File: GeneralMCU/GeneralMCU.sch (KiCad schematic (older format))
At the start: 75 parts, among them J1 ARM_JTAG_SWD, J2 Conn_01x03, J3 USB_B_Micro, J4 Conn_01x04, J5 PWR, J6 OLED, SW1 USER, SW2 RESET, U1 STM32F303R6Tx, U2 SN65HVD230, U3 AZ1117-3.3, Y1 32.768kHz, Y2 8MHz

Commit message: Schematic getting toasty.
99% Percent of symbols added with 90% of footprints filled in, 30% of parts spec'd.

Layout organized by functional group
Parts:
- removed J2: Conn_01x03, symbol Connector_Generic:Conn_01x03
- removed SW1: USER, symbol Switch:SW_Push_Dual
- added C33: 10u, µ104KiCAD_RLC:SMD_pkg_1206, symbol Device:C_Small
- added C34, C35: 1u, µ104KiCAD_RLC:SMD_pkg_0603, symbol Device:C_Small
- added C36: 0.1u, µ104KiCAD_RLC:SMD_pkg_0603, symbol Device:C_Small
- added D6: 5V, LEDs:LED_0603, symbol Device:LED
- added D7: +V, LEDs:LED_0603, symbol Device:LED
- added D8: USB, LEDs:LED_0603, symbol Device:LED
- added D9: ISO5, LEDs:LED_0603, symbol Device:LED
- added F2: 500mA PTC, Diodes_SMD:D_1206, symbol Device:Fuse_Small
- added FB2: FB, µ104KiCAD_RLC:SMD_pkg_0805, symbol Device:Ferrite_Bead_Small
- added JP3: Jumper_NC_Small, Pin_Headers:Pin_Header_Straight_1x02_Pitch2.54mm_SMD_Pin1Left, symbol Device:Jumper_NC_Small
- added Q1: Q_NMOS_DGS, TO_SOT_Packages_SMD:SOT-23, symbol Device:Q_NMOS_GSD
- added R10, R9: 1k, µ104KiCAD_RLC:SMD_pkg_0603, symbol Device:R_Small_US
- added R11, R18, R19, R20, R21: 0, µ104KiCAD_RLC:SMD_pkg_0603, symbol Device:R_Small_US
- added R12, R13, R14, R15, R16, R17: 10k, µ104KiCAD_RLC:SMD_pkg_0603, symbol Device:R_Small_US
- added R22, R23: 4.7k, µ104KiCAD_RLC:SMD_pkg_0603, symbol Device:R_Small_US
- added SW1: USER, Buttons_Switches_SMD:SW_SPST_B3U-1000P, symbol Switch:SW_Push
- added TP2: GND, Measurement_Points:Measurement_Point_Round-SMD-Pad_Small, symbol Connector:TestPoint
- added TP3: 5V, Measurement_Points:Measurement_Point_Round-SMD-Pad_Small, symbol Connector:TestPoint
- added TP4: ISOGND, Measurement_Points:Measurement_Point_Round-SMD-Pad_Small, symbol Connector:TestPoint
- added TP5: +V, Measurement_Points:Measurement_Point_Round-SMD-Pad_Small, symbol Connector:TestPoint
- added TP6: USB, Measurement_Points:Measurement_Point_Round-SMD-Pad_Small, symbol Connector:TestPoint
- added TP7: 5V ISO, Measurement_Points:Measurement_Point_Round-SMD-Pad_Small, symbol Connector:TestPoint
- added U4: P78E05-1000, symbol u104_KICAD_dcdc:V_REG
- added U5: BME280, µ104KiCAD_IC:SOT-363-6, symbol u104_KICAD_sensor:BME280
- added U6: R2S-IIOO-R, symbol u104_KICAD_dcdc:R2S-IIOO-R
- BZ1: footprint (none) -> Buzzer_Beeper:Buzzer_Murata_PKMCS0909E4000-R1
- C1, C10, C11, C12, C13, C14, C15, C16, C17, C18, C19, C2, C20, C21, C3, C30, C31, C4, C5, C6, C7, C8, C9: footprint Capacitors_SMD:C_0603 -> µ104KiCAD_RLC:SMD_pkg_0603
- C22, C23: footprint Capacitors_SMD:C_0603 -> (none)
- C24, C25, C26, C27, C29, C32: footprint Capacitors_SMD:C_1206 -> µ104KiCAD_RLC:SMD_pkg_1206
- C28: value 10u -> 22u; footprint Capacitors_SMD:C_1206 -> µ104KiCAD_RLC:SMD_pkg_1206
- D1: value LED -> 3V3
- D2: footprint LED_SMD:LED_WS2812B_PLCC4_5.0x5.0mm_P3.2mm -> LEDs:LED_WS2812-PLCC6; symbol LED:WS2812B -> LED:WS2812
- FB1: footprint (none) -> µ104KiCAD_RLC:SMD_pkg_0805
- H1, H2, H3, H4: footprint MountingHole:MountingHole_3.2mm_M3_Pad -> (none)
- J3: footprint (none) -> Connectors_USB:USB_Micro-B_Wuerth-629105150521_CircularHoles
- J5: footprint (none) -> Pin_Headers:Pin_Header_Straight_1x02_Pitch2.54mm_SMD_Pin1Left
- J6: footprint (none) -> Pin_Headers:Pin_Header_Straight_1x04_Pitch2.54mm_SMD_Pin1Left
- JP1, JP2: footprint Pin_Headers:Pin_Header_Straight_1x02_Pitch2.54mm -> µ104KiCAD:JUMPER_EGG
- L1: footprint (none) -> µ104KiCAD_RLC:SMD_pkg_1210
- R1, R2, R3, R4, R5, R6: footprint Resistors_SMD:R_0603 -> µ104KiCAD_RLC:SMD_pkg_0603
- R7, R8: footprint Resistors_SMD:R_0603 -> µ104KiCAD_RLC:SMD_pkg_1210
- SB1, SB2, SB3, SB4: footprint µ104KiCAD:JUMPER_EGG -> (none)
- SB5: footprint (none) -> µ104KiCAD:JUMPER_EGG
- SW2: footprint (none) -> Buttons_Switches_SMD:SW_SPST_B3U-1000P; symbol Switch:SW_Push_Dual -> Switch:SW_Push
- TP1: value TestPoint -> 3V3; footprint (none) -> Measurement_Points:Measurement_Point_Round-SMD-Pad_Small
- U3: footprint (none) -> TO_SOT_Packages_SMD:SOT-223-3_TabPin2
- Y1: footprint (none) -> µ104KiCAD_IC:Crystal_NDK_NX3215SA
- Y2: footprint (none) -> µ104KiCAD_IC:Crystal_L5_W3.2
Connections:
- net labels added: VBUS
- wire segments 254 -> 311
- no-connect marks 0 -> 5
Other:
- note added: "- screen and bme280.\n- check nucleo and ref designs\n- make layout like esp or rfm69 modules with solderable pads\n"
- note added: "Drop In PCB Spec:\n1) CAN - Place TVS diode and bus filter caps close to CAN connector\n\n"
- note added: "PARADUINO"
- note added: "PKG\n\n"
- note removed: "- update u104 footprints to new lib\n- check nucleo and ref designs\n- make layout like esp or rfm69 modules with solderable pads\n"
- note removed: "Module\n\n\n"
- note removed: "Node Shield Outline\nOne Node template of a stm32 nucleo shield with all this stuff already on it that we can use for all our designs.\n\n24V Input, all protections\nPower LEDs, RGB User LED\nReset Button, User Button\nSWD Programming Header, Can Term, USB Power Jumpers\nWatchdog, CAN, Piezo, whatever SW wants.\n*Lantronix Eth\n*RS232\n*MicroSD\n*2 Mb EEPROM\n*Loadswitch\n*Possible local Screen.\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"
- note removed: "Receving PCB Spec:\n1) Place TVS diode and bus filter caps close to CAN connector\n\n"
- note removed: "Test Points and LEDs"
- moved on the sheet: BZ1, C24, C26, C28, C29, C30, C31, C32, J1, J3, J6, L1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

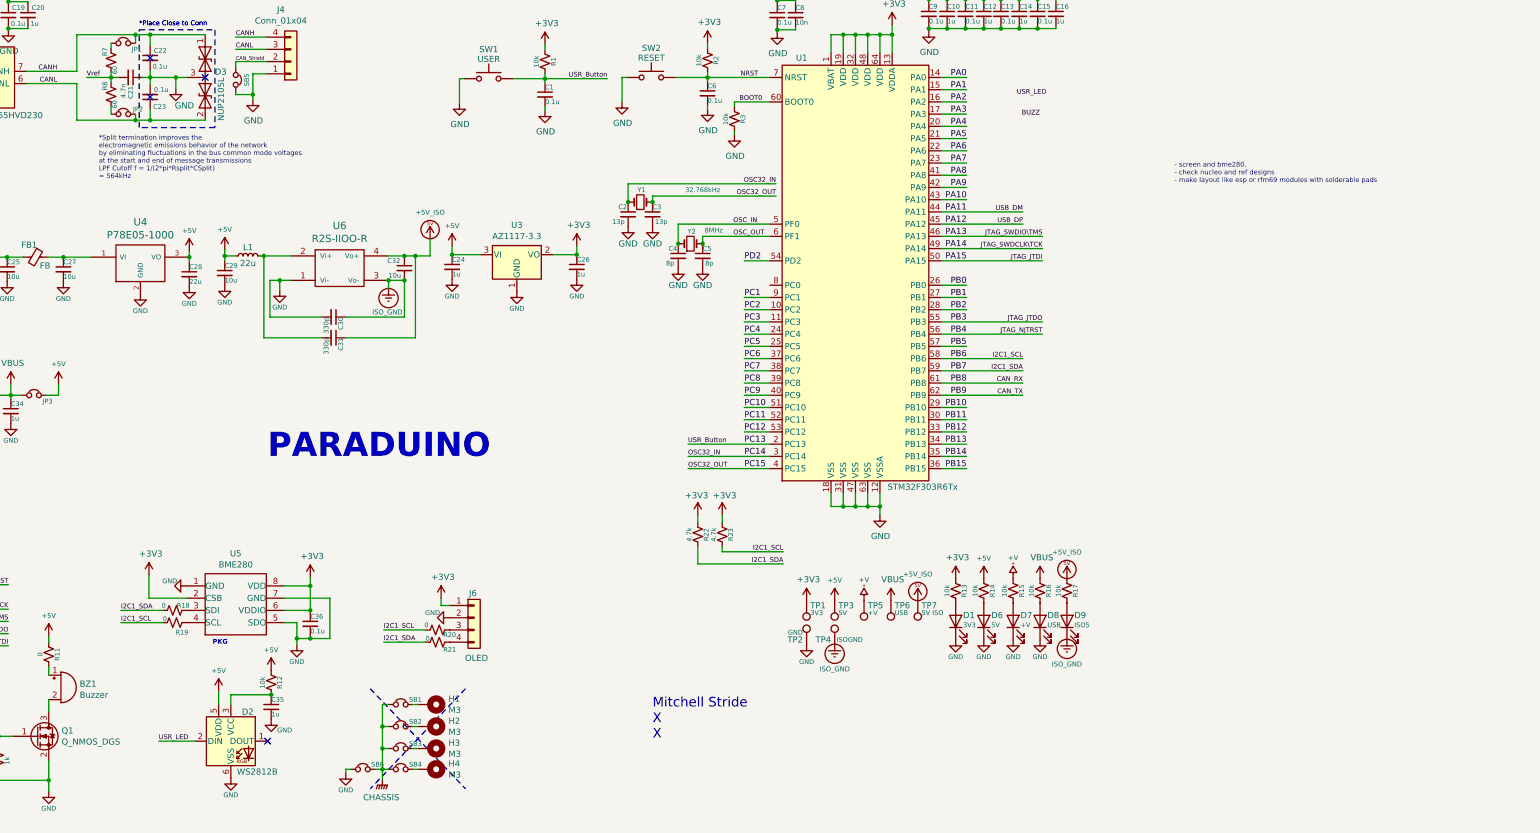
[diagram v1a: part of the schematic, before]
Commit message: Needs castellated pads and sch review
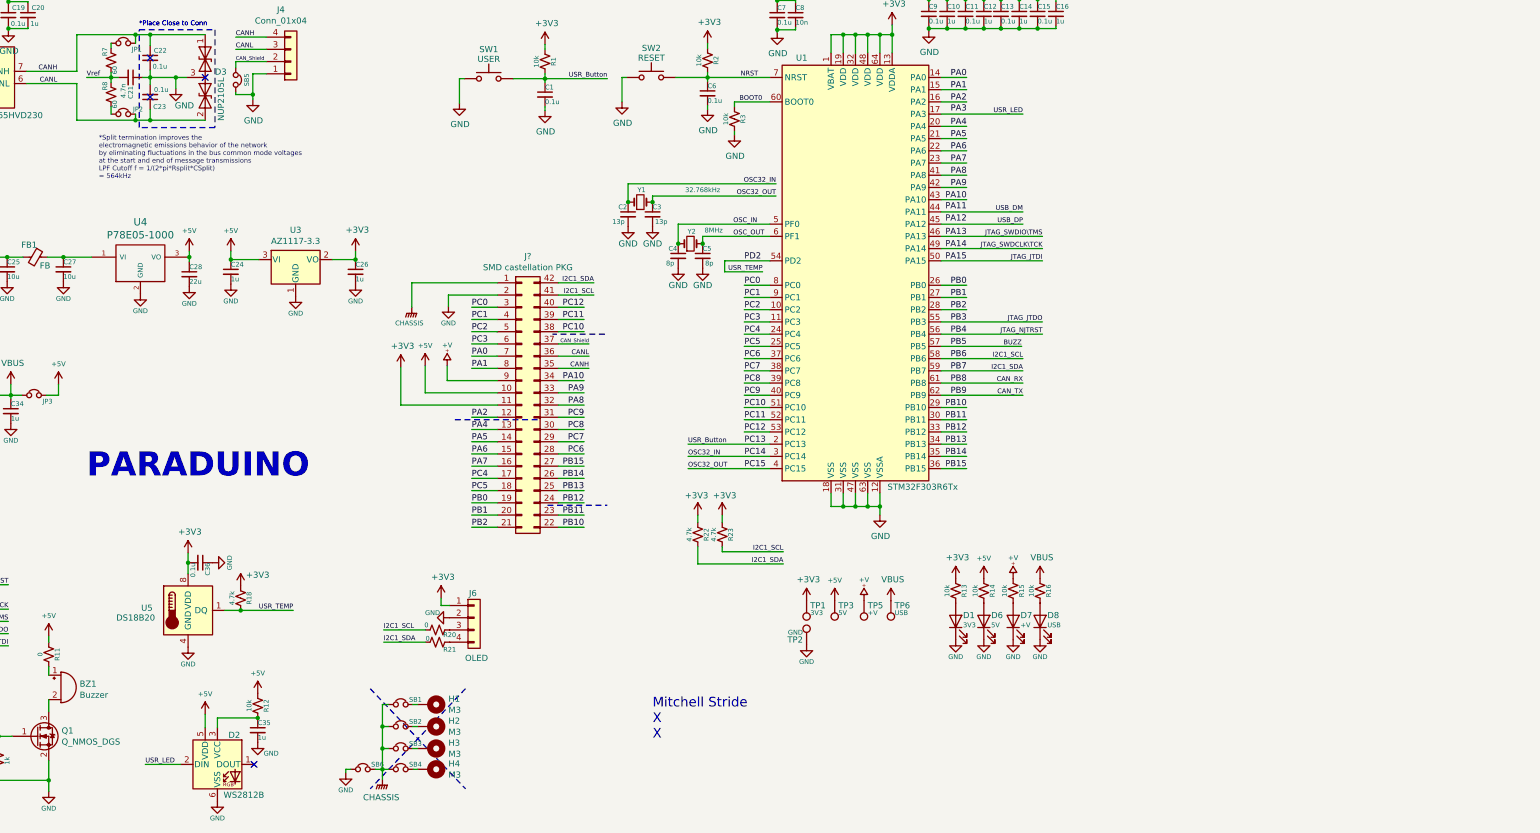
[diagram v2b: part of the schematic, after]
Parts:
- removed C29, C32: 10u, µ104KiCAD_RLC:SMD_pkg_1206, symbol Device:C_Small
- removed C30, C31: 330p, µ104KiCAD_RLC:SMD_pkg_0603, symbol Device:C_Small
- removed D9: ISO5, LEDs:LED_0603, symbol Device:LED
- removed L1: 22u, µ104KiCAD_RLC:SMD_pkg_1210, symbol Device:L_Small
- removed R17: 10k, µ104KiCAD_RLC:SMD_pkg_0603, symbol Device:R_Small_US
- removed R19: 0, µ104KiCAD_RLC:SMD_pkg_0603, symbol Device:R_Small_US
- removed TP4: ISOGND, Measurement_Points:Measurement_Point_Round-SMD-Pad_Small, symbol Connector:TestPoint
- removed TP7: 5V ISO, Measurement_Points:Measurement_Point_Round-SMD-Pad_Small, symbol Connector:TestPoint
- removed U5: BME280, µ104KiCAD_IC:SOT-363-6, symbol u104_KICAD_sensor:BME280
- removed U6: R2S-IIOO-R, symbol u104_KICAD_dcdc:R2S-IIOO-R
- added J?: SMD castellation PKG, symbol Connector_Generic:Conn_02x21_Counter_Clockwise
- added U5: DS18B20, µ104KiCAD_IC:MSOP-8, symbol Sensor_Temperature:DS18B20U
- D4: footprint (none) -> Diodes_SMD:D_SMA
- J6: footprint Pin_Headers:Pin_Header_Straight_1x04_Pitch2.54mm_SMD_Pin1Left -> µ104KiCAD:I2C_OLED
- R18: value 0 -> 4.7k
- U4: footprint (none) -> µ104KiCAD_DCDC:Recom_INNOLINE-R-78E
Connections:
- net PB5 is gone; now on net BUZZ: U1.57 (PB5)
- net +3V3: now also C36.2, R18.2, J?.11 (Pin_11), U5.8 (VDD); no longer C36.1
- net +5V: now also J?.10 (Pin_10)
- net +V: now also J?.9 (Pin_9)
- net CANH: now also J?.35 (Pin_35)
- net CANL: now also J?.36 (Pin_36)
- net CAN_Shield: now also J?.37 (Pin_37)
- net CHASSIS: now also J?.1 (Pin_1)
- net GND: now also C36.1, J?.2 (Pin_2), U5.4 (GND); no longer C36.2
- net I2C1_SCL: now also J?.41 (Pin_41)
- net I2C1_SDA: now also J?.42 (Pin_42); no longer R18.1
- net PA0: now also J?.7 (Pin_7)
- net PA1: now also J?.8 (Pin_8)
- net PA10: now also J?.34 (Pin_34)
- net PA11: no longer J3.2 (D-), U1.44 (PA11)
- net PA12: no longer J3.3 (D+), U1.45 (PA12)
- net PA2: now also J?.12 (Pin_12)
- net PA3: no longer U1.17 (PA3)
- net PA4: now also J?.13 (Pin_13)
- net PA5: now also J?.14 (Pin_14)
- net PA6: now also J?.15 (Pin_15)
- net PA7: now also J?.16 (Pin_16)
- net PA8: now also J?.32 (Pin_32)
- net PA9: now also J?.33 (Pin_33)
- net PB0: now also J?.19 (Pin_19)
- net PB1: now also J?.20 (Pin_20)
- net PB10: now also J?.22 (Pin_22)
- net PB11: now also J?.23 (Pin_23)
- net PB12: now also J?.24 (Pin_24)
- net PB13: now also J?.25 (Pin_25)
- net PB14: now also J?.26 (Pin_26)
- net PB15: now also J?.27 (Pin_27)
- net PB2: now also J?.21 (Pin_21)
- net PC1: now also J?.4 (Pin_4)
- net PC10: now also J?.38 (Pin_38)
- net PC11: now also J?.39 (Pin_39)
- net PC12: now also J?.40 (Pin_40)
- net PC2: now also J?.5 (Pin_5)
- net PC3: now also J?.6 (Pin_6)
- net PC4: now also J?.17 (Pin_17)
- net PC5: now also J?.18 (Pin_18)
- net PC6: now also J?.28 (Pin_28)
- net PC7: now also J?.29 (Pin_29)
- net PC8: now also J?.30 (Pin_30)
- net PC9: now also J?.31 (Pin_31)
- net PD2: now also R18.1, U5.1 (DQ)
- net USR_LED: now also U1.17 (PA3)
- net PC0: now reaches U1.8 (PC0)
- net PC0: now also J?.3 (Pin_3)
- new net USB_DM: J3.2 (D-), U1.44 (PA11)
- new net USB_DP: J3.3 (D+), U1.45 (PA12)
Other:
- note removed: "- screen and bme280.\n- check nucleo and ref designs\n- make layout like esp or rfm69 modules with solderable pads\n"
- note removed: "PKG\n\n"
- moved on the sheet: C24, C26, C35, D2, R12, U3
